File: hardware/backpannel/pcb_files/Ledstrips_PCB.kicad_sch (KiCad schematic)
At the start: 33 parts, among them J1 Conn_01x04_Male, J2 Conn_01x02_Female, U1 AMS1117-3.3, U10 WS2812_ledstrip, U11 WS2812_ledstrip, U12 WS2812_ledstrip, U13 WS2812_ledstrip, U14 WS2812_ledstrip, U15 WS2812_ledstrip, U2 ESP-12E, U3 WS2812_ledstrip, U4 WS2812_ledstrip, U5 WS2812_ledstrip, U6 WS2812_ledstrip, U7 WS2812_ledstrip, U8 WS2812_ledstrip, U9 WS2812_ledstrip

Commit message: PCB in between commit
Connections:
- net +5V: now also J2.1 (Pin_1); no longer J2.2 (Pin_2)
- net GND: now also J2.2 (Pin_2); no longer J2.1 (Pin_1)
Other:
- moved on the sheet: J2
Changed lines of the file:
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@@
+    (stroke (width 0) (type default) (color 0 0 0 0))
+  )
+  (wire (pts (xy 29.21 30.48) (xy 40.64 30.48))
     (stroke (width 0) (type default) (color 0 0 0 0))
   )
@@
   )
   (wire (pts (xy 199.39 35.56) (xy 191.77 35.56))
-    (stroke (width 0) (type default) (color 0 0 0 0))
-  )
-  (wire (pts (xy 29.21 30.48) (xy 40.64 30.48))
     (stroke (width 0) (type default) (color 0 0 0 0))
   )
@@
     (pin "2")
   )
-  (symbol (lib_id "Connector:Conn_01x02_Female") (at 24.13 30.48 180) (unit 1)
-    (in_bom yes) (on_board yes)
-    (property "Reference" "J2" (id 0) (at 26.8732 22.225 0))
-    (property "Value" "Conn_01x02_Female" (id 1) (at 26.8732 24.5364 0))
-    (property "Footprint" "Connector_BarrelJack:BarrelJack_CLIFF_FC681465S_SMT_Horizontal" (id 2) (at 24.13 30.48 0)
-      (effects (font (size 1.27 1.27)) hide)
-    )
-    (property "Datasheet" "~" (id 3) (at 24.13 30.48 0)
-      (effects (font (size 1.27 1.27)) hide)
-    )
+  (symbol (lib_id "Connector:Conn_01x02_Female") (at 24.13 27.94 0) (mirror y) (unit 1)
+    (in_bom yes) (on_board yes)
+    (property "Reference" "J2" (id 0) (at 26.8732 36.195 0))
+    (property "Value" "Conn_01x02_Female" (id 1) (at 26.8732 33.8836 0))
+    (property "Footprint" "Connector_BarrelJack:BarrelJack_CLIFF_FC681465S_SMT_Horizontal" (id 2) (at 24.13 27.94 0)
+      (effects (font (size 1.27 1.27)) hide)
+    )
+    (property "Datasheet" "~" (id 3) (at 24.13 27.94 0)
+      (effects (font (size 1.27 1.27)) hide)
+    )

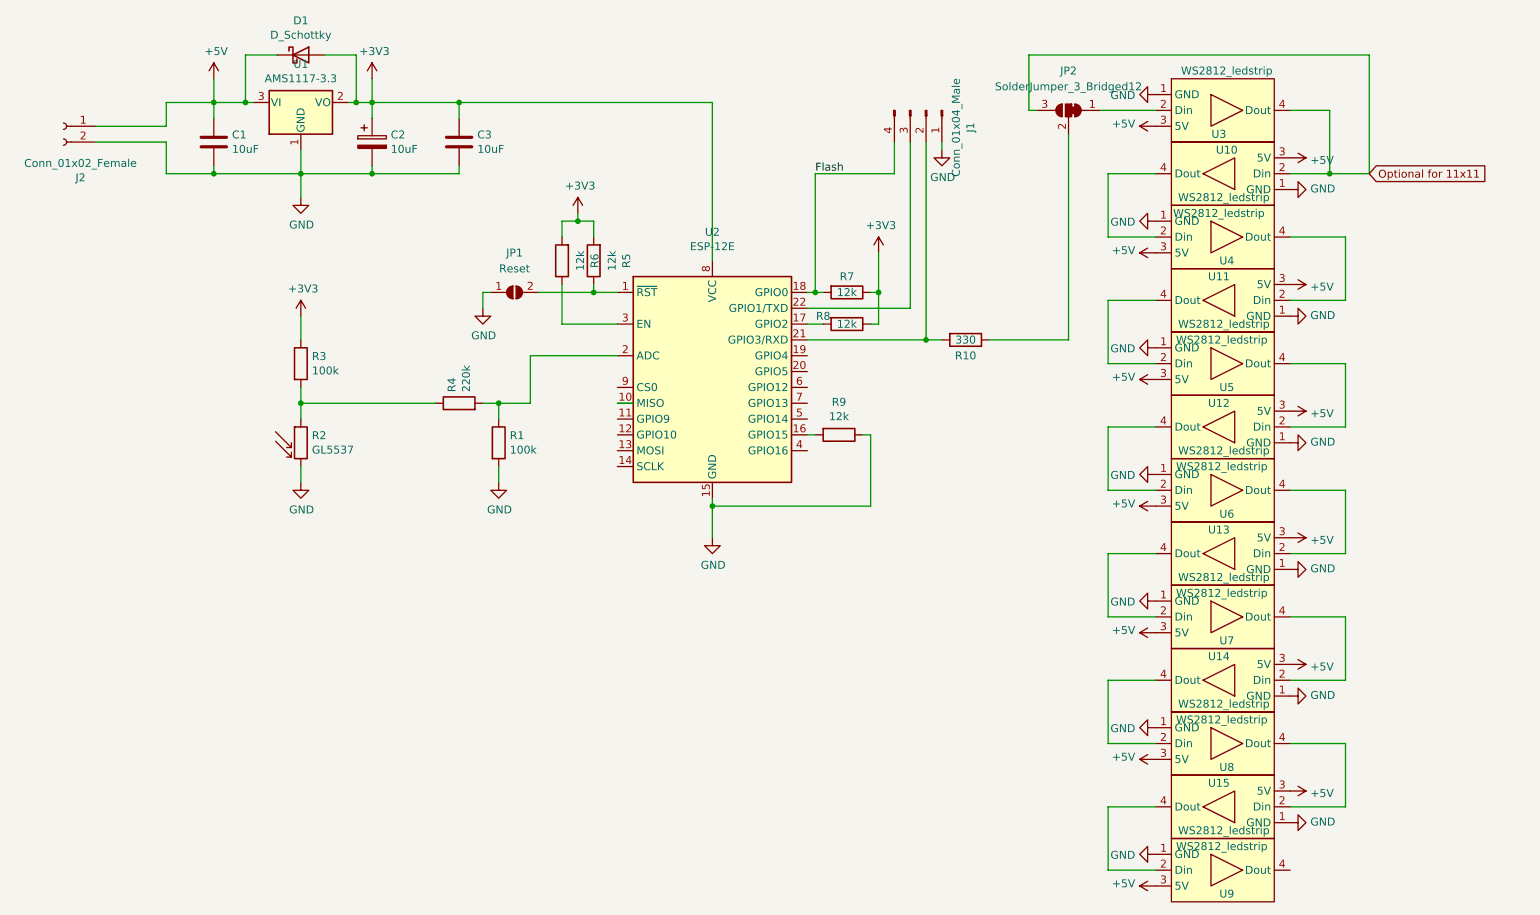
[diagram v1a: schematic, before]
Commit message: Updated PCB and ledschotten
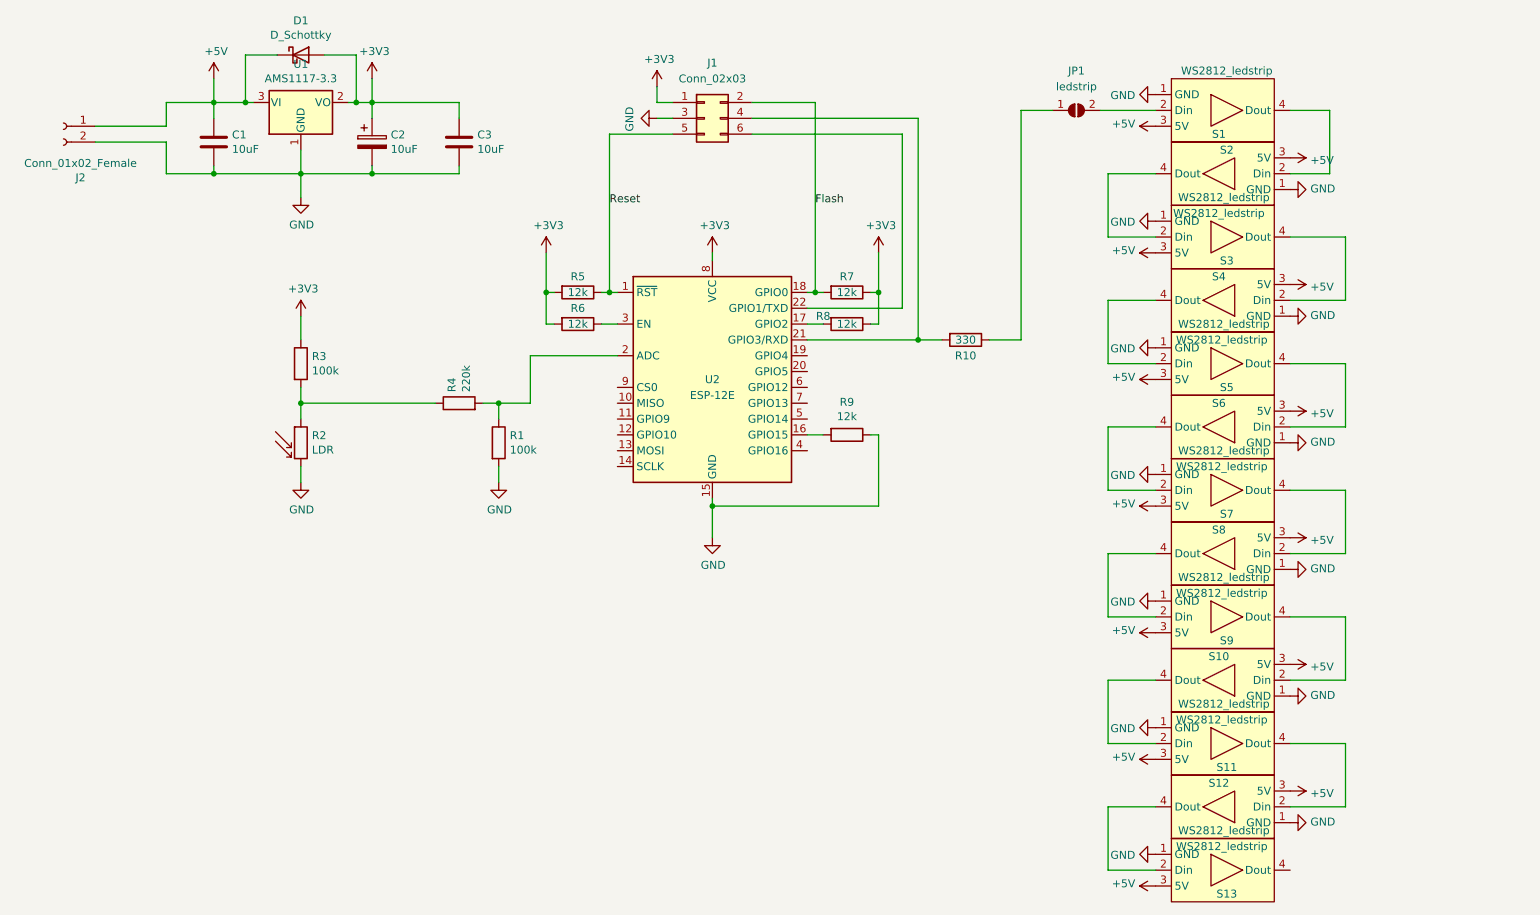
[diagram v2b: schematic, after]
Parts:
- removed J1: Conn_01x04_Male, Connector_PinHeader_2.54mm:PinHeader_1x04_P2.54mm_Vertical, symbol Connector:Conn_01x04_Male
- removed JP2: SolderJumper_3_Bridged12, Jumper:SolderJumper-3_P1.3mm_Bridged12_RoundedPad1.0x1.5mm, symbol Jumper:SolderJumper_3_Bridged12
- added J1: Conn_02x03, Connector_PinHeader_2.54mm:PinHeader_2x03_P2.54mm_Vertical, symbol Connector_Generic:Conn_02x03_Odd_Even
- JP1: value Reset -> ledstrip
- R2: value GL5537 -> LDR; footprint OptoDevice:R_LDR_5.0x4.1mm_P3mm_Vertical -> OptoDevice:R_LDR_5.1x4.3mm_P3.4mm_Vertical
- renumbered U3 to S1, U14 to S10, U8 to S11, U15 to S12, U9 to S13, U10 to S2, U4 to S3, U11 to S4, U5 to S5, U12 to S6, U6 to S7, U13 to S8, U7 to S9
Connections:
- net +3V3: now also J1.1 (Pin_1)
- net Flash: now also J1.2 (Pin_2)
- net GND: now also J1.3 (Pin_3); no longer JP1.1 (A)
- net Reset: now reaches R5.1, U2.1 (~{RST})
- net Reset: now also J1.5 (Pin_5); no longer JP1.2 (B)
- net at R10.2, U2.21 (GPIO3/RXD): now also J1.4 (Pin_4)
- net at U2.22 (GPIO1/TXD): now also J1.6 (Pin_6)
- net at R10.1: now also JP1.1 (A)
- net at S1.2 (Din): now also JP1.2 (B)
- net Optional for 11x11: no longer names the net of S1.4 (Dout), S2.2 (Din)
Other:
- moved on the sheet: R5, R6, R9

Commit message: Finisched PCB
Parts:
- J2: symbol Connector:Conn_01x02_Female -> Connector:Conn_01x03_Female
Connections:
- net GND: now also J2.3 (Pin_3)
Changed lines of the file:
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@@
   (junction (at 144.78 54.61) (diameter 0) (color 0 0 0 0)
   )
+  (junction (at 35.56 30.48) (diameter 0) (color 0 0 0 0)
+  )
   (junction (at 48.26 24.13) (diameter 0) (color 0 0 0 0)
   )
@@
     (stroke (width 0) (type default) (color 0 0 0 0))
   )
-  (wire (pts (xy 29.21 30.48) (xy 40.64 30.48))
+  (wire (pts (xy 29.21 30.48) (xy 35.56 30.48))
     (stroke (width 0) (type default) (color 0 0 0 0))
   )
@@
     (stroke (width 0) (type default) (color 0 0 0 0))
   )
-  (wire (pts (xy 29.21 27.94) (xy 40.64 27.94))
-    (stroke (width 0) (type default) (color 0 0 0 0))
-  )
   (wire (pts (xy 93.98 85.09) (xy 93.98 82.55))
     (stroke (width 0) (type default) (color 0 0 0 0))
@@
     (stroke (width 0) (type default) (color 0 0 0 0))
   )
+  (wire (pts (xy 35.56 30.48) (xy 40.64 30.48))
+    (stroke (width 0) (type default) (color 0 0 0 0))
+  )
   (wire (pts (xy 143.51 62.23) (xy 161.29 62.23))
     (stroke (width 0) (type default) (color 0 0 0 0))
@@
     (stroke (width 0) (type default) (color 0 0 0 0))
   )
+  (wire (pts (xy 35.56 27.94) (xy 35.56 30.48))
+    (stroke (width 0) (type default) (color 0 0 0 0))
+  )
   (wire (pts (xy 62.23 35.56) (xy 62.23 39.37))
     (stroke (width 0) (type default) (color 0 0 0 0))
@@
     (stroke (width 0) (type default) (color 0 0 0 0))
   )
+  (wire (pts (xy 35.56 24.13) (xy 35.56 25.4))
+    (stroke (width 0) (type default) (color 0 0 0 0))
+  )
   (wire (pts (xy 191.77 96.52) (xy 191.77 106.68))
     (stroke (width 0) (type default) (color 0 0 0 0))
@@
     (stroke (width 0) (type default) (color 0 0 0 0))
   )
-  (wire (pts (xy 40.64 24.13) (xy 48.26 24.13))
+  (wire (pts (xy 35.56 24.13) (xy 48.26 24.13))
     (stroke (width 0) (type default) (color 0 0 0 0))
   )
@@
     (stroke (width 0) (type default) (color 0 0 0 0))
   )
+  (wire (pts (xy 29.21 27.94) (xy 35.56 27.94))
+    (stroke (width 0) (type default) (color 0 0 0 0))
+  )
   (wire (pts (xy 99.06 64.77) (xy 113.03 64.77))
     (stroke (width 0) (type default) (color 0 0 0 0))
@@
     (stroke (width 0) (type default) (color 0 0 0 0))
   )
+  (wire (pts (xy 35.56 25.4) (xy 29.21 25.4))
+    (stroke (width 0) (type default) (color 0 0 0 0))
+  )
   (wire (pts (xy 172.72 62.23) (xy 177.8 62.23))
     (stroke (width 0) (type default) (color 0 0 0 0))
@@
   )
   (wire (pts (xy 229.87 116.84) (xy 220.98 116.84))
-    (stroke (width 0) (type default) (color 0 0 0 0))
-  )
-  (wire (pts (xy 40.64 27.94) (xy 40.64 24.13))
     (stroke (width 0) (type default) (color 0 0 0 0))
   )
@@
     (pin "2")
   )
-  (symbol (lib_id "Connector:Conn_01x02_Female") (at 24.13 27.94 0) (mirror y) (unit 1)
+  (symbol (lib_id "Connector:Conn_01x03_Female") (at 24.13 27.94 0) (mirror y) (unit 1)
     (in_bom yes) (on_board yes)
     (property "Reference" "J2" (id 0) (at 26.8732 36.195 0))
@@
     (pin "1")
     (pin "2")
+    (pin "3")
   )
   (symbol (lib_id "power:+5V") (at 48.26 20.32 0) (unit 1)
